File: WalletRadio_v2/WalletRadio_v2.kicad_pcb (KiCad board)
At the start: 2 copper layers, 92.3 x 52.8 mm, 43 parts, among them J1 UJC-HP-3-SMT-TR, Q1 BSP315P, Q2 Q_NPN_ECB, SW1 SW_SPDT, SW2 CUS-13TB, U1 MCP73831-2-OT, U2 Si4824, U3 LM324A

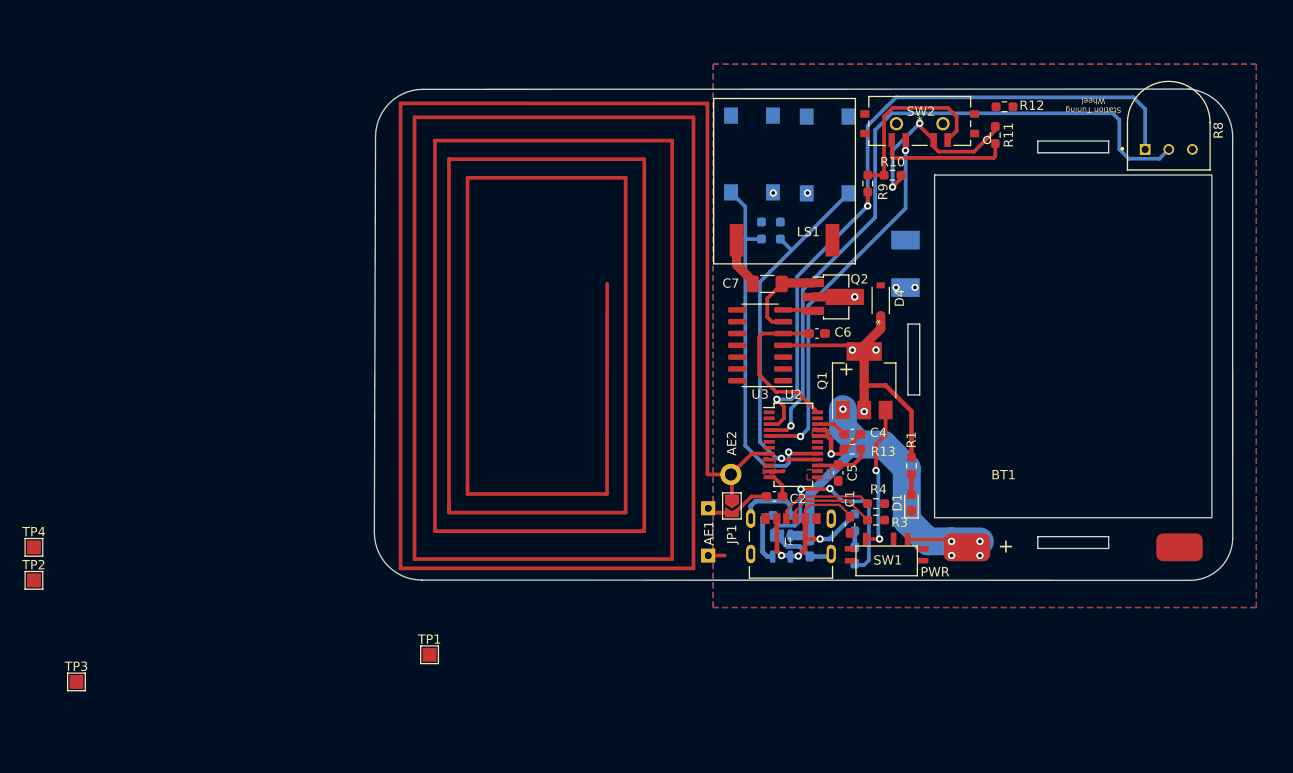
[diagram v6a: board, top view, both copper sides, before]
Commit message: More layout. Added fields for BOM creation.
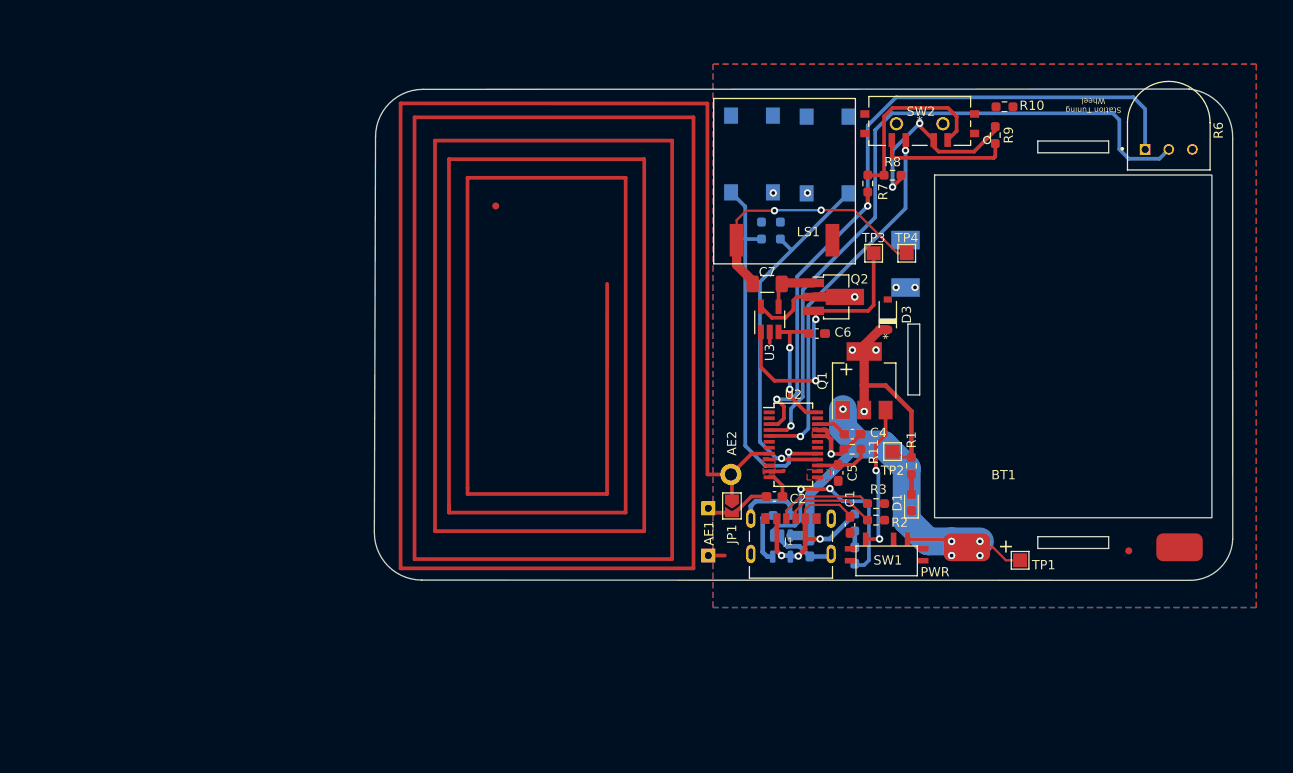
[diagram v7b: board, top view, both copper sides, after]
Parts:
- removed the D4 at (157.7, 99.1)
- added D3: KDZVTFTR3.3B, WalletRadio:KDZVTFTR3.3B, F.Cu at (158.5, 100.6)
- added FID1: Fiducial, Fiducial:Fiducial_0.75mm_Mask2.25mm, F.Cu at (116.3, 88.9)
- added FID2: Fiducial, Fiducial:Fiducial_0.75mm_Mask2.25mm, F.Cu at (184.4, 126.0)
- U3: value LM324A -> MCP6476; footprint Package_SO:SOIC-14_3.9x8.7mm_P1.27mm -> Package_TO_SOT_SMD:SOT-23-5_HandSoldering
- moved TP4 99.0 mm to (160.5, 94.0)
- moved TP3 97.3 mm to (157.0, 94.0)
- moved TP2 93.4 mm to (159.0, 115.3)
- moved TP1 64.3 mm to (172.7, 127.0)
- moved U3 2.98 mm to (145.8, 101.1), turned to 90 degrees
- renumbered D3 to D4, R12 to R10, R13 to R11, R14 to R12, R15 to R13, R3 to R2, R4 to R3, R5 to R4, R7 to R5, R8 to R6, R9 to R7, R10 to R8, R11 to R9
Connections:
- U3 pad 1: (no net) -> Net-(Q2-Pad3)
- U3 pad 2: (no net) -> GND
- U3 pad 3: (no net) -> Net-(C6-Pad1)
- U3 pad 4: /+Vbat -> Net-(C7-Pad2)
- U3 pad 5: Net-(C6-Pad1) -> /+Vbat
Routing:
- net Net-(Q2-Pad3): track 3.29 -> 30.4 mm, vias 0 -> 2
- net Net-(C7-Pad1): track 5.41 -> 28.2 mm, vias 0 -> 2
- net /raw_Vbat: track 48.4 -> 54.7 mm
- net Net-(C7-Pad2): track 9.57 -> 6.04 mm
- net Net-(C6-Pad1): track 17.9 -> 15.2 mm, vias 0 -> 2
- net /+Vbat: track 43.4 -> 45.1 mm
- net GND: track 17.2 -> 18.4 mm

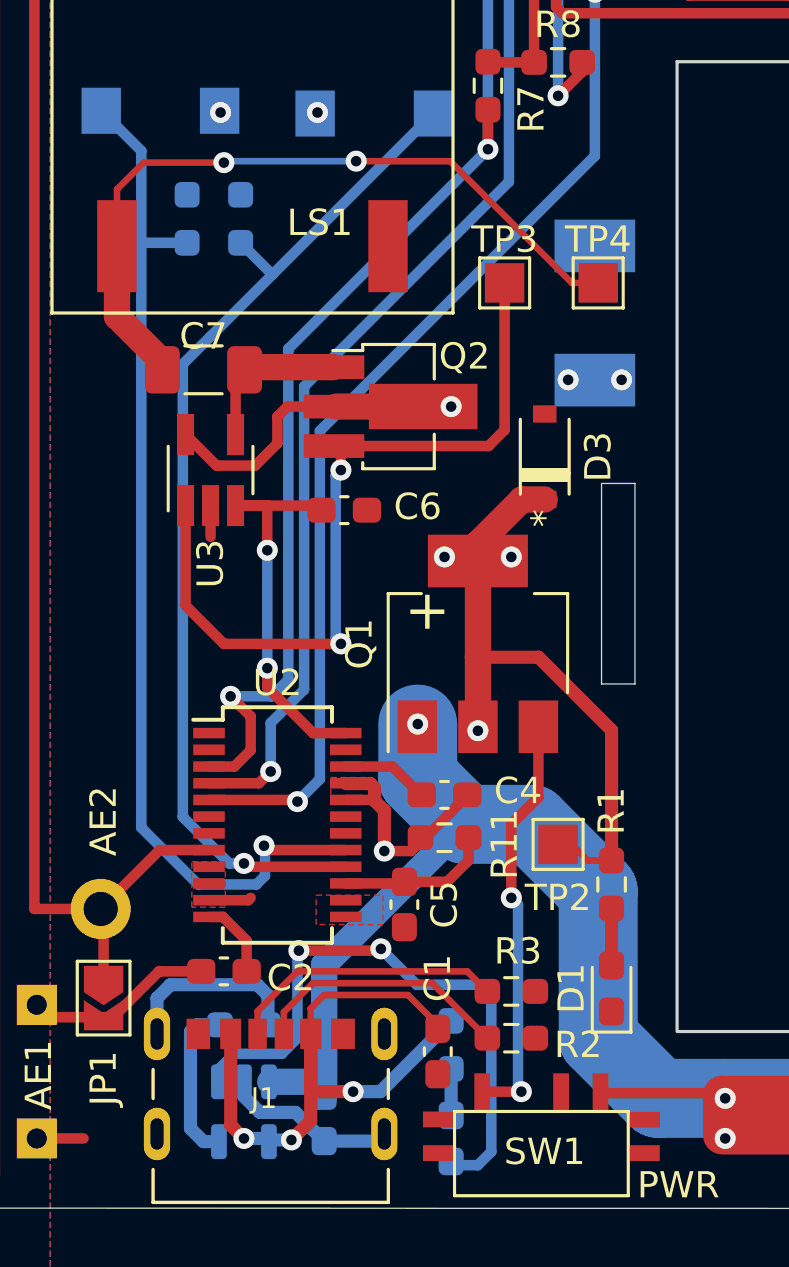
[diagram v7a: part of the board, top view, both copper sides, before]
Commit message: Had to change some components because they were out of stock
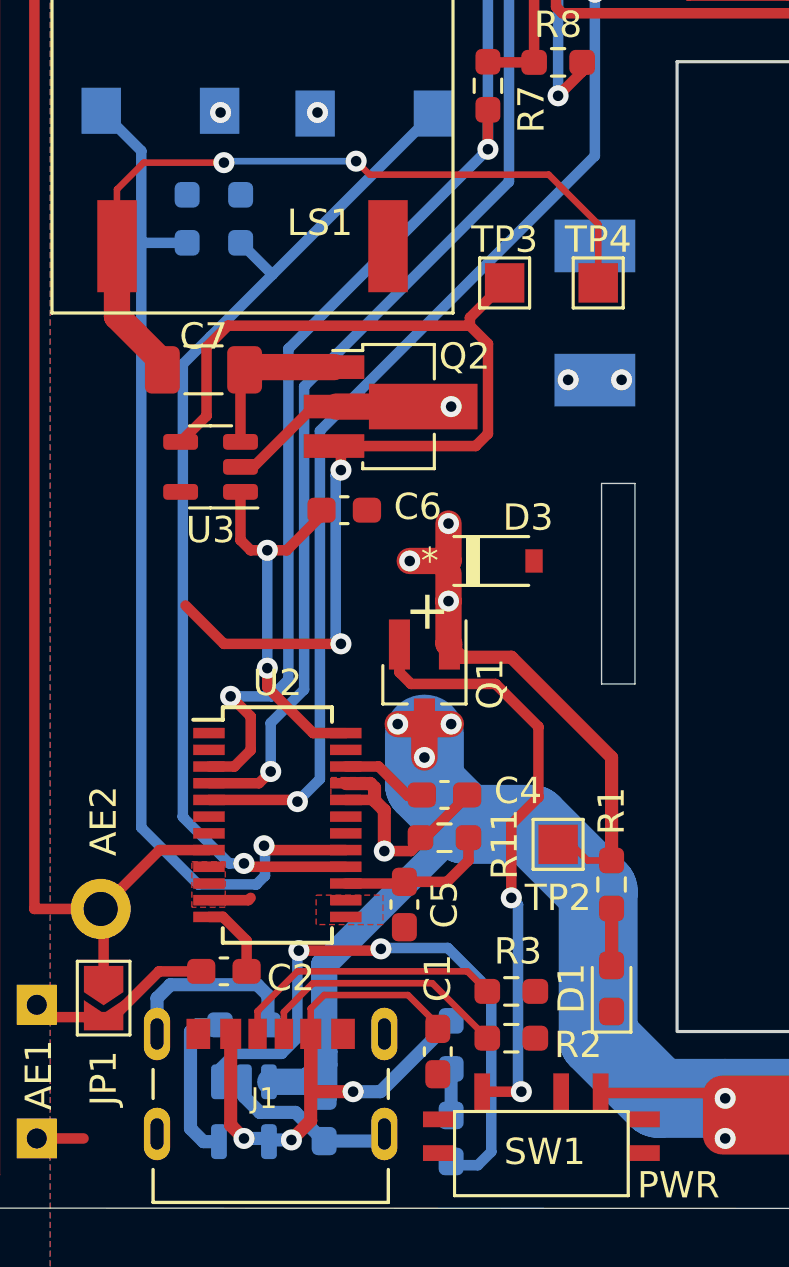
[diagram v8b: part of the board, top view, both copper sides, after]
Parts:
- C6: value 0.1uF -> 0.1u
- D3: value KDZVTFTR3.3B -> KDZVTFTR3.0B
- Q1: value BSP315P -> DMP212LQ-7; footprint Package_TO_SOT_SMD:SOT-223 -> Package_TO_SOT_SMD:SOT-23_Handsoldering
- U3: value MCP6476 -> AZV321KTR-G1; footprint Package_TO_SOT_SMD:SOT-23-5_HandSoldering -> Package_TO_SOT_SMD:SOT-23-5
- moved D3 4.45 mm to (156.5, 104.5), turned to 0 degrees
- moved Q1 2.54 mm to (153.9, 109.2), turned to -90 degrees
- moved U3 0.12 mm to (145.8, 101.0), turned to 180 degrees
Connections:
- Q1 pad 1: /raw_Vbat -> /+Vbat
- Q1 pad 2: /+Vbat -> Net-(Q1-Pad2)
- Q1 pad 3: Net-(Q1-Pad3) -> /raw_Vbat
- SW1 pad 2: Net-(Q1-Pad3) -> Net-(Q1-Pad2)
- U3 pad 1: Net-(Q2-Pad3) -> Net-(C6-Pad1)
- U3 pad 2: GND -> /+Vbat
- U3 pad 3: Net-(C6-Pad1) -> Net-(C7-Pad2)
- U3 pad 4: Net-(C7-Pad2) -> Net-(Q2-Pad3)
- U3 pad 5: /+Vbat -> GND
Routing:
- net Net-(Q1-Pad2): track 0.00 -> 23.2 mm, vias 0 -> 2
- net Net-(Q1-Pad3): track 16.0 -> 0.00 mm, vias 2 -> 0
- net Net-(Q2-Pad3): track 30.4 -> 41.3 mm
- net /+Vbat: track 45.1 -> 37.7 mm
- net /raw_Vbat: track 54.7 -> 58.3 mm, vias 5 -> 7
- net Net-(C7-Pad1): track 28.2 -> 29.5 mm
- net GND: track 18.4 -> 17.2 mm
